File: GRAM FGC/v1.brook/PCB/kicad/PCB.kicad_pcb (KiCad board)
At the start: 2 copper layers, 288.8 x 160.1 mm, 24 parts, among them J1 USB_C_Receptacle_USB2.0_16P, SW1 SW_Push, SW2 SW_Push, SW3 SW_Push, SW4 SW_Push

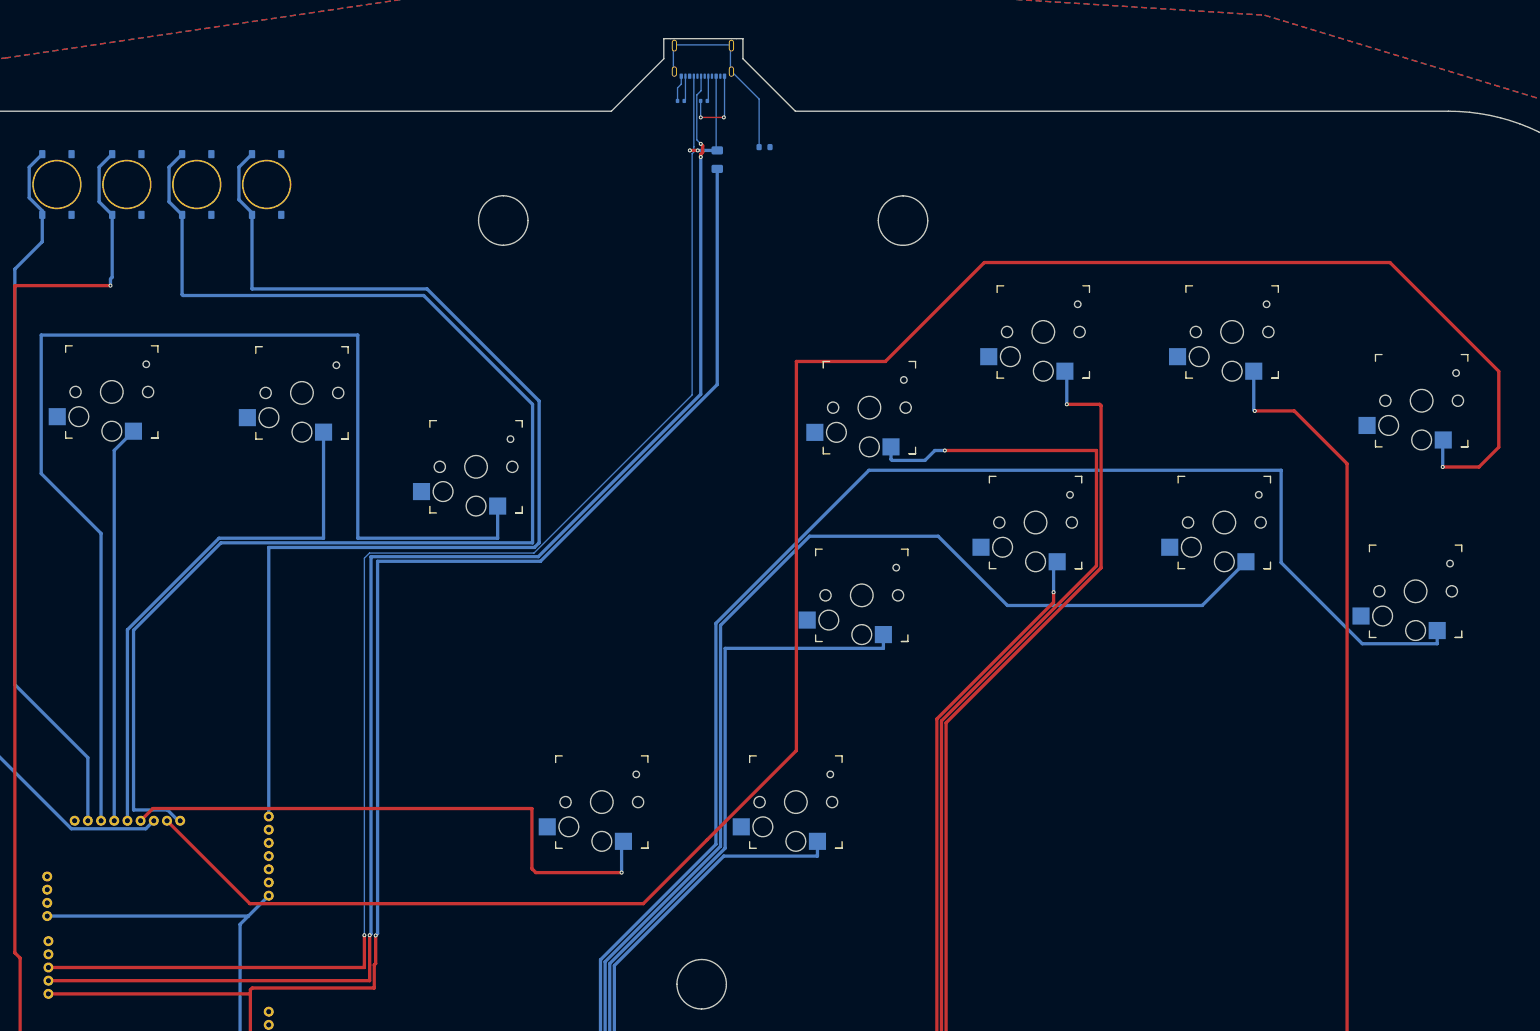
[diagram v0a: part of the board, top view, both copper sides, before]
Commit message: Fixed connections, top panel & gerbers
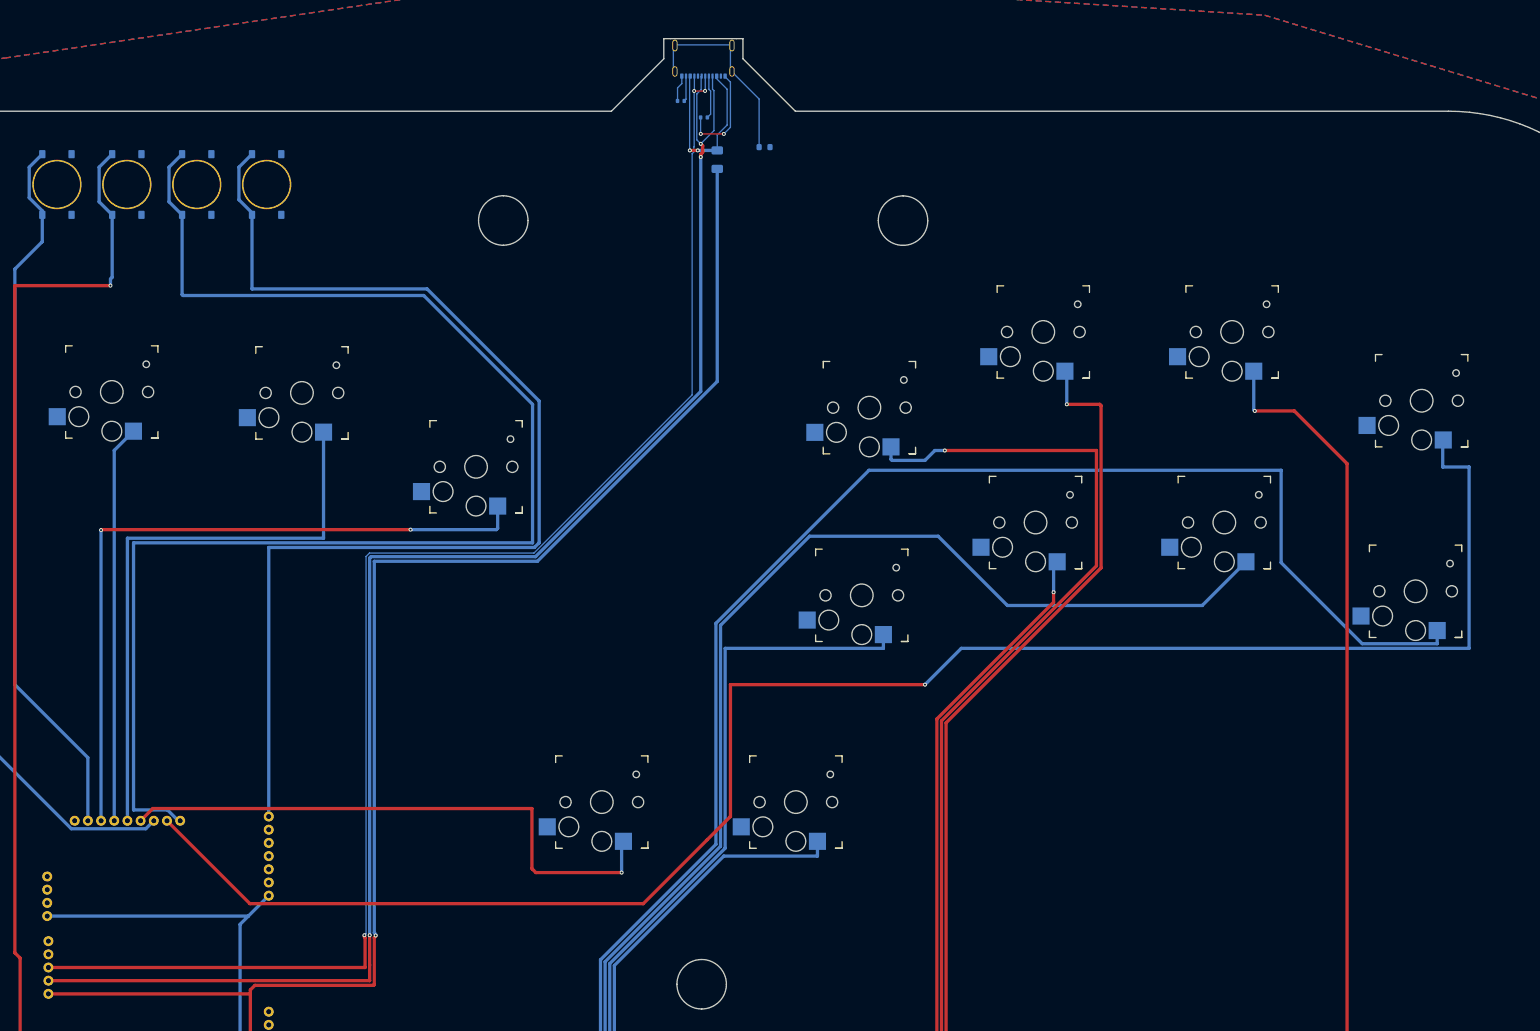
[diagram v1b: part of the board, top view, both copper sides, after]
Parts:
- moved R2 2.50 mm to (218.5, 59.0)
- moved J1 0.09 mm to (218.4, 50.3)
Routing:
- net Right: track 182.3 -> 107.7 mm, vias 0 -> 2
- net L1: track 314.3 -> 266.1 mm
- net Net-(F1-Pad1): track 16.2 -> 28.7 mm
- net D-: track 222.3 -> 233.3 mm
- net Down: track 80.5 -> 88.7 mm
- net PS: track 205.0 -> 212.7 mm
- net D+: track 218.4 -> 222.6 mm, vias 1 -> 3
- net GND: track 16.4 -> 19.6 mm
- net Net-(J1-CC2): track 3.81 -> 6.58 mm

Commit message: Final working version
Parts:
- removed F1: 500 mA, Fuse:Fuse_1206_3216Metric
- removed J1: USB_C_Receptacle_USB2.0_16P, PCM_marbastlib-xp-various:USB_C_Receptacle_HRO_TYPE-C-31-M-23
- removed R1, R2: 5.1k, Resistor_SMD:R_0402_1005Metric
- removed R3: 1M, Resistor_SMD:R_0603_1608Metric
- added R4: 5.1k, Resistor_SMD:R_0805_2012Metric, B.Cu at (223.1, 60.0)
- added R5: 5.1k, Resistor_SMD:R_0805_2012Metric, B.Cu at (215.4, 57.2)
- added USB1: HRO-TYPE-C-31-M-12, Type-C:HRO-TYPE-C-31-M-12, B.Cu at (218.4, 45.8)
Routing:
- net Net-(J1-SHIELD): track 29.9 -> 0.00 mm
- net Net-(F1-Pad1): track 28.7 -> 0.00 mm, vias 2 -> 0
- net +5V: track 220.7 -> 240.6 mm, vias 1 -> 3
- net GND: track 19.6 -> 8.10 mm, vias 2 -> 0
- net Net-(USB1-CC2): track 0.00 -> 8.78 mm
- net D-: track 233.3 -> 241.0 mm, vias 3 -> 1
- net Net-(J1-CC2): track 6.58 -> 0.00 mm
- net D+: track 222.6 -> 227.6 mm, vias 3 -> 4
- net Net-(USB1-CC1): track 0.00 -> 4.28 mm
- net Net-(J1-CC1): track 3.88 -> 0.00 mm
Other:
- board text added: "P5 Mini Custom GRAM by GOOBY.SPACE"
- board text removed: "P5 Mini Custom GRAM"
